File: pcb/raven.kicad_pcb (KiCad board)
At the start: 4 copper layers, 0 parts

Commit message: Finish schematic
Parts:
- added C1: 100u, Capacitor_SMD:C_Elec_8x6.2, F.Cu at (206.4, 74.2)
- added C10: 100n, Capacitor_SMD:C_0402_1005Metric, F.Cu at (135.8, 156.5)
- added C11: 220n, Capacitor_SMD:C_0402_1005Metric, F.Cu at (135.8, 158.5)
- added C12: 4u7, Capacitor_SMD:C_0603_1608Metric, F.Cu at (139.2, 159.3)
- added C13: 100u, Capacitor_SMD:C_Elec_8x6.2, F.Cu at (222.6, 74.2)
- added C14: 100n, Capacitor_SMD:C_0402_1005Metric, F.Cu at (215.4, 66.6)
- added C15: 2u2, Capacitor_SMD:C_0402_1005Metric, F.Cu at (226.4, 65.0)
- added C16: 100n, Capacitor_SMD:C_0402_1005Metric, F.Cu at (216.4, 66.6)
- added C17: 22n, Capacitor_SMD:C_0402_1005Metric, F.Cu at (215.4, 68.6)
- added C18: 100u, Capacitor_SMD:C_Elec_8x6.2, F.Cu at (238.8, 74.2)
- added C19: 100n, Capacitor_SMD:C_0402_1005Metric, F.Cu at (231.6, 66.6)
- added C2: 100n, Capacitor_SMD:C_0402_1005Metric, F.Cu at (199.2, 66.6)
- added C20: 2u2, Capacitor_SMD:C_0402_1005Metric, F.Cu at (242.6, 65.0)
- added C21: 100n, Capacitor_SMD:C_0402_1005Metric, F.Cu at (232.6, 66.6)
- added C22: 22n, Capacitor_SMD:C_0402_1005Metric, F.Cu at (231.6, 68.6)
- added C23: 100u, Capacitor_SMD:C_Elec_8x6.2, F.Cu at (255.0, 74.2)
- added C24: 100n, Capacitor_SMD:C_0402_1005Metric, F.Cu at (247.8, 66.6)
- added C25: 2u2, Capacitor_SMD:C_0402_1005Metric, F.Cu at (258.8, 65.0)
- added C26: 100n, Capacitor_SMD:C_0402_1005Metric, F.Cu at (248.8, 66.6)
- added C27: 22n, Capacitor_SMD:C_0402_1005Metric, F.Cu at (247.8, 68.6)
- added C28: 100n, Capacitor_SMD:C_0402_1005Metric, F.Cu at (89.6, 117.8)
- added C29: 100n, Capacitor_SMD:C_0402_1005Metric, F.Cu at (93.2, 154.5)
- added C3: 2u2, Capacitor_SMD:C_0402_1005Metric, F.Cu at (210.2, 65.0)
- added C30: 100n, Capacitor_SMD:C_0402_1005Metric, F.Cu at (93.2, 156.5)
- added C31: 100n, Capacitor_SMD:C_0402_1005Metric, F.Cu at (93.2, 158.5)
- added C32: 12p, Capacitor_SMD:C_0402_1005Metric, F.Cu at (93.2, 160.4)
- added C33: 12p, Capacitor_SMD:C_0402_1005Metric, F.Cu at (93.2, 162.4)
- added C34: 100n, Capacitor_SMD:C_0402_1005Metric, F.Cu at (93.2, 164.4)
- added C35: 100n, Capacitor_SMD:C_0402_1005Metric, F.Cu at (96.1, 154.5)
- added C36: 100n, Capacitor_SMD:C_0402_1005Metric, F.Cu at (96.1, 156.5)
- added C37: 1u, Capacitor_SMD:C_0402_1005Metric, F.Cu at (96.1, 158.5)
- added C38: 1u, Capacitor_SMD:C_0402_1005Metric, F.Cu at (96.1, 160.4)
- added C39: 100n, Capacitor_SMD:C_0402_1005Metric, F.Cu at (96.1, 162.4)
- added C4: 100n, Capacitor_SMD:C_0402_1005Metric, F.Cu at (200.2, 66.6)
- added C40: 100n, Capacitor_SMD:C_0402_1005Metric, F.Cu at (129.7, 154.5)
- added C41: 100n, Capacitor_SMD:C_0402_1005Metric, F.Cu at (129.7, 156.5)
- added C42: 100n, Capacitor_SMD:C_0402_1005Metric, F.Cu at (129.7, 158.5)
- added C43: 100n, Capacitor_SMD:C_0402_1005Metric, F.Cu at (129.7, 160.4)
- added C44: 100n, Capacitor_SMD:C_0402_1005Metric, F.Cu at (129.7, 162.4)
- added C45: 100n, Capacitor_SMD:C_0402_1005Metric, F.Cu at (155.2, 93.7)
- added C46: 100n, Capacitor_SMD:C_0402_1005Metric, F.Cu at (155.2, 95.7)
- added C47: 100n, Capacitor_SMD:C_0402_1005Metric, F.Cu at (155.2, 97.6)
- added C48: 100n, Capacitor_SMD:C_0402_1005Metric, F.Cu at (155.2, 99.6)
- added C49: 100n, Capacitor_SMD:C_0402_1005Metric, F.Cu at (155.2, 101.6)
- added C5: 22n, Capacitor_SMD:C_0402_1005Metric, F.Cu at (199.2, 68.6)
- added C50: 100n, Capacitor_SMD:C_0402_1005Metric, F.Cu at (108.2, 117.5)
- added C51: 100n, Capacitor_SMD:C_0402_1005Metric, F.Cu at (108.2, 119.5)
- added C52: 100n, Capacitor_SMD:C_0402_1005Metric, F.Cu at (108.2, 121.4)
- added C53: 100n, Capacitor_SMD:C_0402_1005Metric, F.Cu at (108.2, 123.4)
- added C54: 100n, Capacitor_SMD:C_0402_1005Metric, F.Cu at (108.2, 125.4)
- added C55: 100n, Capacitor_SMD:C_0402_1005Metric, F.Cu at (131.7, 117.5)
- added C56: 100n, Capacitor_SMD:C_0402_1005Metric, F.Cu at (131.7, 119.5)
- added C57: 100n, Capacitor_SMD:C_0402_1005Metric, F.Cu at (131.7, 121.4)
- added C58: 100n, Capacitor_SMD:C_0402_1005Metric, F.Cu at (131.7, 123.4)
- added C59: 100n, Capacitor_SMD:C_0402_1005Metric, F.Cu at (131.7, 125.4)
- added C6: 2u2, Capacitor_SMD:C_0402_1005Metric, F.Cu at (86.7, 122.7)
- added C60: 100n, Capacitor_SMD:C_0402_1005Metric, F.Cu at (155.2, 111.4)
- added C61: 100n, Capacitor_SMD:C_0402_1005Metric, F.Cu at (155.2, 113.4)
- added C62: 100n, Capacitor_SMD:C_0402_1005Metric, F.Cu at (155.2, 115.3)
- added C63: 100n, Capacitor_SMD:C_0402_1005Metric, F.Cu at (155.2, 117.3)
- added C64: 100n, Capacitor_SMD:C_0402_1005Metric, F.Cu at (155.2, 119.3)
- added C65: 100u, Capacitor_SMD:C_Elec_8x6.2, F.Cu at (190.2, 74.2)
- added C66: 100n, Capacitor_SMD:C_0402_1005Metric, F.Cu at (183.0, 66.6)
- added C67: 2u2, Capacitor_SMD:C_0402_1005Metric, F.Cu at (194.0, 65.0)
- added C68: 100n, Capacitor_SMD:C_0402_1005Metric, F.Cu at (184.0, 66.6)
- added C69: 22n, Capacitor_SMD:C_0402_1005Metric, F.Cu at (183.0, 68.6)
- added C7: 100n, Capacitor_SMD:C_0402_1005Metric, F.Cu at (86.7, 124.7)
- added C8: 100n, Capacitor_SMD:C_0402_1005Metric, F.Cu at (86.7, 126.7)
- added C9: 2u2, Capacitor_SMD:C_0402_1005Metric, F.Cu at (135.8, 154.5)
- added D1: GLED, LED_SMD:LED_0603_1608Metric, F.Cu at (83.0, 78.6)
- added D10: RLED, LED_SMD:LED_0603_1608Metric, F.Cu at (244.8, 66.8)
- added D11: WLED, LED_SMD:LED_0603_1608Metric, F.Cu at (261.0, 70.0)
- added D12: GLED, LED_SMD:LED_0603_1608Metric, F.Cu at (261.0, 68.4)
- added D13: RLED, LED_SMD:LED_0603_1608Metric, F.Cu at (261.0, 66.8)
- added D14: WLED, LED_SMD:LED_0603_1608Metric, F.Cu at (111.8, 166.4)
- added D15: RLED, LED_SMD:LED_0603_1608Metric, F.Cu at (111.8, 169.0)
- added D16: WLED, LED_SMD:LED_0603_1608Metric, F.Cu at (130.3, 164.7)
- added D17: WLED, LED_SMD:LED_0603_1608Metric, F.Cu at (130.3, 167.3)
- added D18: WLED, LED_SMD:LED_0603_1608Metric, F.Cu at (155.8, 103.8)
- added D19: WLED, LED_SMD:LED_0603_1608Metric, F.Cu at (155.8, 106.4)
- added D2: WLED, LED_SMD:LED_0603_1608Metric, F.Cu at (212.4, 70.0)
- added D20: WLED, LED_SMD:LED_0603_1608Metric, F.Cu at (108.8, 127.7)
- added D21: WLED, LED_SMD:LED_0603_1608Metric, F.Cu at (108.8, 130.2)
- added D22: WLED, LED_SMD:LED_0603_1608Metric, F.Cu at (132.3, 127.7)
- added D23: WLED, LED_SMD:LED_0603_1608Metric, F.Cu at (132.3, 130.2)
- added D24: WLED, LED_SMD:LED_0603_1608Metric, F.Cu at (155.8, 121.5)
- added D25: WLED, LED_SMD:LED_0603_1608Metric, F.Cu at (155.8, 124.1)
- added D26: WLED, LED_SMD:LED_0603_1608Metric, F.Cu at (196.2, 70.0)
- added D27: GLED, LED_SMD:LED_0603_1608Metric, F.Cu at (196.2, 68.4)
- added D28: RLED, LED_SMD:LED_0603_1608Metric, F.Cu at (196.2, 66.8)
- added D3: GLED, LED_SMD:LED_0603_1608Metric, F.Cu at (212.4, 68.4)
- added D4: RLED, LED_SMD:LED_0603_1608Metric, F.Cu at (212.4, 66.8)
- added D5: WLED, LED_SMD:LED_0603_1608Metric, F.Cu at (228.6, 70.0)
- added D6: GLED, LED_SMD:LED_0603_1608Metric, F.Cu at (228.6, 68.4)
- added D7: RLED, LED_SMD:LED_0603_1608Metric, F.Cu at (228.6, 66.8)
- added D8: WLED, LED_SMD:LED_0603_1608Metric, F.Cu at (244.8, 70.0)
- added D9: GLED, LED_SMD:LED_0603_1608Metric, F.Cu at (244.8, 68.4)
- added FB1: FerriteBead, Inductor_SMD:L_0805_2012Metric, F.Cu at (94.1, 171.2)
- added H1: MountingHole_Pad, MountingHole:MountingHole_2.5mm_Pad, F.Cu at (40.0, 50.0)
- added H2: MountingHole_Pad, MountingHole:MountingHole_2.5mm_Pad, F.Cu at (98.0, 50.0)
- added H3: MountingHole_Pad, MountingHole:MountingHole_2.5mm_Pad, F.Cu at (116.2, 93.7)
- added H4: MountingHole_Pad, MountingHole:MountingHole_2.5mm_Pad, F.Cu at (116.2, 100.2)
- added J1: Conn_02x20_Odd_Even, Connector_PinHeader_2.54mm:PinHeader_2x20_P2.54mm_Vertical, F.Cu at (44.9, 51.3)
- added J10: Conn_01x02_Pin, Connector_PinHeader_2.54mm:PinHeader_1x02_P2.54mm_Vertical, F.Cu at (76.0, 124.1)
- added J11: Screw_Terminal_01x02, TerminalBlock_Phoenix:TerminalBlock_Phoenix_MKDS-1,5-2_1x02_P5.00mm_Horizontal, F.Cu at (223.4, 58.1)
- added J12: Screw_Terminal_01x02, TerminalBlock_Phoenix:TerminalBlock_Phoenix_MKDS-1,5-2_1x02_P5.00mm_Horizontal, F.Cu at (239.6, 58.1)
- added J13: Screw_Terminal_01x02, TerminalBlock_Phoenix:TerminalBlock_Phoenix_MKDS-1,5-2_1x02_P5.00mm_Horizontal, F.Cu at (255.8, 58.1)
- added J14: Conn_01x04_Pin, Connector_PinHeader_2.54mm:PinHeader_1x04_P2.54mm_Vertical, F.Cu at (123.0, 155.9)
- added J15: Conn_01x04_Pin, Connector_PinHeader_2.54mm:PinHeader_1x04_P2.54mm_Vertical, F.Cu at (148.5, 95.0)
- added J16: Conn_01x04_Pin, Connector_PinHeader_2.54mm:PinHeader_1x04_P2.54mm_Vertical, F.Cu at (101.5, 118.8)
- added J17: Conn_01x04_Pin, Connector_PinHeader_2.54mm:PinHeader_1x04_P2.54mm_Vertical, F.Cu at (125.0, 118.8)
- added J18: Conn_01x04_Pin, Connector_PinHeader_2.54mm:PinHeader_1x04_P2.54mm_Vertical, F.Cu at (148.5, 112.7)
- added J19: Screw_Terminal_01x02, TerminalBlock_Phoenix:TerminalBlock_Phoenix_MKDS-1,5-2_1x02_P5.00mm_Horizontal, F.Cu at (191.0, 58.3)
- added J2: Conn_01x04_MountingPin, Connector_JST:JST_SH_SM04B-SRSS-TB_1x04-1MP_P1.00mm_Horizontal, F.Cu at (85.3, 73.5)
- added J20: Conn_01x02_Pin, Connector_PinHeader_2.54mm:PinHeader_1x02_P2.54mm_Vertical, F.Cu at (148.4, 167.6)
- added J21: Conn_01x03_Pin, Connector_PinHeader_2.54mm:PinHeader_1x03_P2.54mm_Vertical, F.Cu at (162.1, 95.0)
- added J22: Conn_01x03_Pin, Connector_PinHeader_2.54mm:PinHeader_1x03_P2.54mm_Vertical, F.Cu at (136.6, 166.4)
- added J23: Conn_01x03_Pin, Connector_PinHeader_2.54mm:PinHeader_1x03_P2.54mm_Vertical, F.Cu at (76.0, 103.2)
- added J24: Conn_01x03_Pin, Connector_PinHeader_2.54mm:PinHeader_1x03_P2.54mm_Vertical, F.Cu at (162.1, 112.7)
- added J25: Conn_01x03_Pin, Connector_PinHeader_2.54mm:PinHeader_1x03_P2.54mm_Vertical, F.Cu at (155.1, 155.9)
- added J26: Conn_01x03_Pin, Connector_PinHeader_2.54mm:PinHeader_1x03_P2.54mm_Vertical, F.Cu at (148.4, 155.9)
- added J3: Screw_Terminal_01x02, TerminalBlock_Phoenix:TerminalBlock_Phoenix_MKDS-1,5-2_1x02_P5.00mm_Horizontal, F.Cu at (214.8, 100.0)
- added J4: Screw_Terminal_01x02, TerminalBlock_Phoenix:TerminalBlock_Phoenix_MKDS-1,5-2_1x02_P5.00mm_Horizontal, F.Cu at (187.8, 99.2)
- added J5: Screw_Terminal_01x02, TerminalBlock_Phoenix:TerminalBlock_Phoenix_MKDS-1,5-2_1x02_P5.00mm_Horizontal, F.Cu at (207.2, 58.1)
- added J6: Conn_01x02_Pin, Connector_PinHeader_2.54mm:PinHeader_1x02_P2.54mm_Vertical, F.Cu at (82.7, 103.2)
- added J7: Conn_01x02_Pin, Connector_PinHeader_2.54mm:PinHeader_1x02_P2.54mm_Vertical, F.Cu at (155.8, 130.4)
- added J8: Conn_01x02_Pin, Connector_PinHeader_2.54mm:PinHeader_1x02_P2.54mm_Vertical, F.Cu at (76.0, 114.9)
- added J9: Conn_01x02_Pin, Connector_PinHeader_2.54mm:PinHeader_1x02_P2.54mm_Vertical, F.Cu at (144.3, 130.4)
- added Q1: AO3400A, Package_TO_SOT_SMD:SOT-23, F.Cu at (87.5, 103.3)
- added Q2: AO3400A, Package_TO_SOT_SMD:SOT-23, F.Cu at (160.6, 130.5)
- added Q3: AO3400A, Package_TO_SOT_SMD:SOT-23, F.Cu at (80.8, 115.0)
- added Q4: AO3400A, Package_TO_SOT_SMD:SOT-23, F.Cu at (149.0, 130.5)
- added Q5: AO3400A, Package_TO_SOT_SMD:SOT-23, F.Cu at (80.8, 124.2)
- added Q6: AO3400A, Package_TO_SOT_SMD:SOT-23, F.Cu at (153.2, 167.6)
- added R1: 1k, Resistor_SMD:R_0402_1005Metric, F.Cu at (86.4, 78.3)
- added R10: 1k, Resistor_SMD:R_0402_1005Metric, F.Cu at (227.4, 65.0)
- added R11: 1k, Resistor_SMD:R_0402_1005Metric, F.Cu at (226.0, 68.2)
- added R12: 1k, Resistor_SMD:R_0402_1005Metric, F.Cu at (225.4, 65.0)
- added R13: 1k, Resistor_SMD:R_0402_1005Metric, F.Cu at (229.0, 65.4)
- added R14: 1k, Resistor_SMD:R_0402_1005Metric, F.Cu at (242.2, 69.2)
- added R15: 1k, Resistor_SMD:R_0402_1005Metric, F.Cu at (243.6, 65.0)
- added R16: 1k, Resistor_SMD:R_0402_1005Metric, F.Cu at (242.2, 68.2)
- added R17: 1k, Resistor_SMD:R_0402_1005Metric, F.Cu at (241.6, 65.0)
- added R18: 1k, Resistor_SMD:R_0402_1005Metric, F.Cu at (245.2, 65.4)
- added R19: 1k, Resistor_SMD:R_0402_1005Metric, F.Cu at (258.4, 69.2)
- added R2: 1k, Resistor_SMD:R_0402_1005Metric, F.Cu at (209.8, 69.2)
- added R20: 1k, Resistor_SMD:R_0402_1005Metric, F.Cu at (259.8, 65.0)
- added R21: 1k, Resistor_SMD:R_0402_1005Metric, F.Cu at (258.4, 68.2)
- added R22: 1k, Resistor_SMD:R_0402_1005Metric, F.Cu at (257.8, 65.0)
- added R23: 1k, Resistor_SMD:R_0402_1005Metric, F.Cu at (261.4, 65.4)
- added R24: 10k, Resistor_SMD:R_0402_1005Metric, F.Cu at (86.7, 117.8)
- added R25: R_Photo, Resistor_SMD:R_1210_3225Metric, F.Cu at (88.1, 114.7)
- added R26: 1k, Resistor_SMD:R_0402_1005Metric, F.Cu at (108.3, 166.2)
- added R27: 1k, Resistor_SMD:R_0402_1005Metric, F.Cu at (108.3, 168.1)
- added R28: 1k, Resistor_SMD:R_0402_1005Metric, F.Cu at (108.3, 170.1)
- added R29: 1k, Resistor_SMD:R_0402_1005Metric, F.Cu at (126.8, 154.5)
- added R3: 1k, Resistor_SMD:R_0402_1005Metric, F.Cu at (211.2, 65.0)
- added R30: 1k, Resistor_SMD:R_0402_1005Metric, F.Cu at (126.8, 156.5)
- added R31: 1k, Resistor_SMD:R_0402_1005Metric, F.Cu at (126.8, 158.5)
- added R32: 1k, Resistor_SMD:R_0402_1005Metric, F.Cu at (126.8, 160.5)
- added R33: 1k, Resistor_SMD:R_0402_1005Metric, F.Cu at (126.8, 162.5)
- added R34: 1k, Resistor_SMD:R_0402_1005Metric, F.Cu at (126.8, 164.5)
- added R35: 1k, Resistor_SMD:R_0402_1005Metric, F.Cu at (152.3, 93.7)
- added R36: 1k, Resistor_SMD:R_0402_1005Metric, F.Cu at (152.3, 95.7)
- added R37: 1k, Resistor_SMD:R_0402_1005Metric, F.Cu at (152.3, 97.7)
- added R38: 1k, Resistor_SMD:R_0402_1005Metric, F.Cu at (152.3, 99.7)
- added R39: 1k, Resistor_SMD:R_0402_1005Metric, F.Cu at (152.3, 101.7)
- added R4: 1k, Resistor_SMD:R_0402_1005Metric, F.Cu at (209.8, 68.2)
- added R40: 1k, Resistor_SMD:R_0402_1005Metric, F.Cu at (152.3, 103.6)
- added R41: 1k, Resistor_SMD:R_0402_1005Metric, F.Cu at (105.3, 117.5)
- added R42: 1k, Resistor_SMD:R_0402_1005Metric, F.Cu at (105.3, 119.5)
- added R43: 1k, Resistor_SMD:R_0402_1005Metric, F.Cu at (105.3, 121.5)
- added R44: 1k, Resistor_SMD:R_0402_1005Metric, F.Cu at (105.3, 123.5)
- added R45: 1k, Resistor_SMD:R_0402_1005Metric, F.Cu at (105.3, 125.5)
- added R46: 1k, Resistor_SMD:R_0402_1005Metric, F.Cu at (105.3, 127.5)
- added R47: 1k, Resistor_SMD:R_0402_1005Metric, F.Cu at (128.8, 117.5)
- added R48: 1k, Resistor_SMD:R_0402_1005Metric, F.Cu at (128.8, 119.5)
- added R49: 1k, Resistor_SMD:R_0402_1005Metric, F.Cu at (128.8, 121.5)
- added R5: 1k, Resistor_SMD:R_0402_1005Metric, F.Cu at (209.2, 65.0)
- added R50: 1k, Resistor_SMD:R_0402_1005Metric, F.Cu at (128.8, 123.5)
- added R51: 1k, Resistor_SMD:R_0402_1005Metric, F.Cu at (128.8, 125.5)
- added R52: 1k, Resistor_SMD:R_0402_1005Metric, F.Cu at (128.8, 127.5)
- added R53: 1k, Resistor_SMD:R_0402_1005Metric, F.Cu at (152.3, 111.4)
- added R54: 1k, Resistor_SMD:R_0402_1005Metric, F.Cu at (152.3, 113.4)
- added R55: 1k, Resistor_SMD:R_0402_1005Metric, F.Cu at (152.3, 115.4)
- added R56: 1k, Resistor_SMD:R_0402_1005Metric, F.Cu at (152.3, 117.4)
- added R57: 1k, Resistor_SMD:R_0402_1005Metric, F.Cu at (152.3, 119.4)
- added R58: 1k, Resistor_SMD:R_0402_1005Metric, F.Cu at (152.3, 121.3)
- added R59: 1k, Resistor_SMD:R_0402_1005Metric, F.Cu at (193.6, 69.2)
- added R6: 1k, Resistor_SMD:R_0402_1005Metric, F.Cu at (212.8, 65.4)
- added R60: 1k, Resistor_SMD:R_0402_1005Metric, F.Cu at (195.0, 65.0)
- added R61: 1k, Resistor_SMD:R_0402_1005Metric, F.Cu at (193.6, 68.2)
- added R62: 1k, Resistor_SMD:R_0402_1005Metric, F.Cu at (193.0, 65.0)
- added R63: 1k, Resistor_SMD:R_0402_1005Metric, F.Cu at (196.6, 65.4)
- added R7: 2k2, Resistor_SMD:R_0402_1005Metric, F.Cu at (142.7, 159.1)
- added R8: 2k2, Resistor_SMD:R_0402_1005Metric, F.Cu at (142.7, 161.1)
- added R9: 1k, Resistor_SMD:R_0402_1005Metric, F.Cu at (226.0, 69.2)
- added U1: DRV8874PWPR, Package_SO:HTSSOP-16-1EP_4.4x5mm_P0.65mm_EP3.4x5mm_Mask2.46x2.31mm, F.Cu at (204.7, 66.9)
- added U10: 74AUP1G373, Package_TO_SOT_SMD:SOT-363_SC-70-6, F.Cu at (118.6, 155.5)
- added U11: 74AUP1G373, Package_TO_SOT_SMD:SOT-363_SC-70-6, F.Cu at (118.6, 159.5)
- added U12: 74LVC1G08, Package_TO_SOT_SMD:SOT-353_SC-70-5, F.Cu at (118.6, 163.4)
- added U13: 74LVC1G08, Package_TO_SOT_SMD:SOT-353_SC-70-5, F.Cu at (118.6, 167.3)
- added U14: 74AUP1G373, Package_TO_SOT_SMD:SOT-363_SC-70-6, F.Cu at (144.1, 94.7)
- added U15: 74AUP1G373, Package_TO_SOT_SMD:SOT-363_SC-70-6, F.Cu at (144.1, 98.6)
- added U16: 74LVC1G08, Package_TO_SOT_SMD:SOT-353_SC-70-5, F.Cu at (144.1, 102.5)
- added U17: 74LVC1G08, Package_TO_SOT_SMD:SOT-353_SC-70-5, F.Cu at (144.1, 106.5)
- added U18: 74AUP1G373, Package_TO_SOT_SMD:SOT-363_SC-70-6, F.Cu at (97.1, 118.5)
- added U19: 74AUP1G373, Package_TO_SOT_SMD:SOT-363_SC-70-6, F.Cu at (97.1, 122.4)
- added U2: ICM-42688-P, Package_LGA:LGA-14_3x2.5mm_P0.5mm_LayoutBorder3x4y, F.Cu at (90.4, 123.9)
- added U20: 74LVC1G08, Package_TO_SOT_SMD:SOT-353_SC-70-5, F.Cu at (97.1, 126.4)
- added U21: 74LVC1G08, Package_TO_SOT_SMD:SOT-353_SC-70-5, F.Cu at (97.1, 130.3)
- added U22: 74AUP1G373, Package_TO_SOT_SMD:SOT-363_SC-70-6, F.Cu at (120.6, 118.5)
- added U23: 74AUP1G373, Package_TO_SOT_SMD:SOT-363_SC-70-6, F.Cu at (120.6, 122.4)
- added U24: 74LVC1G08, Package_TO_SOT_SMD:SOT-353_SC-70-5, F.Cu at (120.6, 126.4)
- added U25: 74LVC1G08, Package_TO_SOT_SMD:SOT-353_SC-70-5, F.Cu at (120.6, 130.3)
- added U26: 74AUP1G373, Package_TO_SOT_SMD:SOT-363_SC-70-6, F.Cu at (144.1, 112.4)
- added U27: 74AUP1G373, Package_TO_SOT_SMD:SOT-363_SC-70-6, F.Cu at (144.1, 116.3)
- added U28: 74LVC1G08, Package_TO_SOT_SMD:SOT-353_SC-70-5, F.Cu at (144.1, 120.2)
- added U29: 74LVC1G08, Package_TO_SOT_SMD:SOT-353_SC-70-5, F.Cu at (144.1, 124.2)
- added U3: QMC5883L, Package_LGA:LGA-16_3x3mm_P0.5mm, F.Cu at (139.8, 155.8)
- added U30: DRV8874PWPR, Package_SO:HTSSOP-16-1EP_4.4x5mm_P0.65mm_EP3.4x5mm_Mask2.46x2.31mm, F.Cu at (188.5, 66.9)
- added U4: DRV8874PWPR, Package_SO:HTSSOP-16-1EP_4.4x5mm_P0.65mm_EP3.4x5mm_Mask2.46x2.31mm, F.Cu at (220.9, 66.9)
- added U5: DRV8874PWPR, Package_SO:HTSSOP-16-1EP_4.4x5mm_P0.65mm_EP3.4x5mm_Mask2.46x2.31mm, F.Cu at (237.1, 66.9)
- added U6: DRV8874PWPR, Package_SO:HTSSOP-16-1EP_4.4x5mm_P0.65mm_EP3.4x5mm_Mask2.46x2.31mm, F.Cu at (253.3, 66.9)
- added U7: STM32G431CBUx, Package_DFN_QFN:QFN-48-1EP_7x7mm_P0.5mm_EP5.6x5.6mm, F.Cu at (102.2, 169.8)
- added U8: 74HC595, Package_SO:SOIC-16_3.9x9.9mm_P1.27mm, F.Cu at (101.8, 159.4)
- added U9: 74HC595, Package_SO:SOIC-16_3.9x9.9mm_P1.27mm, F.Cu at (110.2, 159.4)
- added Y1: 16MHz, Crystal:Crystal_SMD_3225-4Pin_3.2x2.5mm, F.Cu at (94.4, 167.6)

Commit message: Save progress
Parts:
- removed C18, C23, C65: 100u, Capacitor_SMD:C_Elec_8x6.2
- removed C39, C41, C42, C43, C44, C46, C47, C48, C49, C51, C52, C53, C54, C56, C57, C58, C59, C61, C62, C63, C64: 100n, Capacitor_SMD:C_0402_1005Metric
- removed D14, D17, D18, D19, D20, D21, D22, D23, D24, D25: WLED, LED_SMD:LED_0603_1608Metric
- removed D15: RLED, LED_SMD:LED_0603_1608Metric
- removed J10, J20, J6, J7, J8, J9: Conn_01x02_Pin, Connector_PinHeader_2.54mm:PinHeader_1x02_P2.54mm_Vertical
- removed J12, J13, J19, J5: Screw_Terminal_01x02, TerminalBlock_Phoenix:TerminalBlock_Phoenix_MKDS-1,5-2_1x02_P5.00mm_Horizontal
- removed Q1, Q2, Q3, Q4, Q5, Q6: AO3400A, Package_TO_SOT_SMD:SOT-23
- removed R26, R33, R34, R39, R40, R45, R46, R51, R52, R57, R58: 1k, Resistor_SMD:R_0402_1005Metric
- removed U10, U11, U14, U15, U18, U19, U22, U23, U26, U27: 74AUP1G373, Package_TO_SOT_SMD:SOT-363_SC-70-6
- removed U12, U13, U16, U17, U20, U21, U24, U25, U28, U29: 74LVC1G08, Package_TO_SOT_SMD:SOT-353_SC-70-5
- removed U9: 74HC595, Package_SO:SOIC-16_3.9x9.9mm_P1.27mm
- J1: footprint Connector_PinHeader_2.54mm:PinHeader_2x20_P2.54mm_Vertical -> Connector_PinSocket_2.54mm:PinSocket_2x20_P2.54mm_Vertical; moved to B.Cu
- J11: value Screw_Terminal_01x02 -> Screw_Terminal_01x10; footprint TerminalBlock_Phoenix:TerminalBlock_Phoenix_MKDS-1,5-2_1x02_P5.00mm_Horizontal -> TerminalBlock_Phoenix:TerminalBlock_Phoenix_MKDS-1,5-10_1x10_P5.00mm_Horizontal
- R7, R8: value 2k2 -> 10k
- moved R28 134.9 mm to (127.6, 36.6)
- moved C34 130.8 mm to (122.9, 37.0)
- moved D16 129.8 mm to (109.9, 36.5)
- moved C29 126.9 mm to (123.3, 31.2)
- moved C30 126.9 mm to (123.3, 33.2)
- moved C31 126.9 mm to (123.3, 35.1)
- moved J11 123.2 mm to (106.5, 96.9), turned to 0 degrees
- moved J22 111.9 mm to (138.6, 54.5)
- moved U7 111.1 mm to (119.4, 60.0), turned to 45 degrees
- moved FB1 109.7 mm to (124.9, 65.9), turned to -45 degrees
- moved R7 109.2 mm to (104.4, 56.8), turned to -90 degrees
- moved R8 109.2 mm to (104.4, 58.8), turned to 90 degrees
- moved R23 107.3 mm to (155.3, 81.5), turned to 90 degrees
- moved C12 105.9 mm to (110.0, 57.6), turned to 180 degrees
- moved C11 105.7 mm to (111.2, 55.6), turned to 90 degrees
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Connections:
- net /MotorHub/ERCTL renamed /MotorHub/SCTL
- net /MotorHub/Encoder10/A renamed /MotorHub/Encoder5/A
- net /MotorHub/Encoder10/AIN renamed /MotorHub/Encoder5/AIN
- net /MotorHub/Encoder10/B renamed /MotorHub/Encoder5/B
- net /MotorHub/Encoder10/BIN renamed /MotorHub/Encoder5/BIN
- net /MotorHub/Encoder6/A renamed /MotorHub/Encoder1/A
- net /MotorHub/Encoder6/AIN renamed /MotorHub/Encoder1/AIN
- net /MotorHub/Encoder6/B renamed /MotorHub/Encoder1/B
- net /MotorHub/Encoder6/BIN renamed /MotorHub/Encoder1/BIN
- net /MotorHub/Encoder7/A renamed /MotorHub/Encoder2/A
- net /MotorHub/Encoder7/AIN renamed /MotorHub/Encoder2/AIN
- net /MotorHub/Encoder7/B renamed /MotorHub/Encoder2/B
- net /MotorHub/Encoder7/BIN renamed /MotorHub/Encoder2/BIN
- net /MotorHub/Encoder8/A renamed /MotorHub/Encoder3/A
- net /MotorHub/Encoder8/AIN renamed /MotorHub/Encoder3/AIN
- net /MotorHub/Encoder8/B renamed /MotorHub/Encoder3/B
- net /MotorHub/Encoder8/BIN renamed /MotorHub/Encoder3/BIN
- net /MotorHub/Encoder9/A renamed /MotorHub/Encoder4/A
- net /MotorHub/Encoder9/AIN renamed /MotorHub/Encoder4/AIN
- net /MotorHub/Encoder9/B renamed /MotorHub/Encoder4/B
- net /MotorHub/Encoder9/BIN renamed /MotorHub/Encoder4/BIN
- net /MotorHub/PHDAT renamed /MotorHub/RDAT
- net /MotorHub/SCLK renamed /MotorHub/RCLK
- net /MotorHub/SSV renamed /MotorHub/RSV
- net Net-(U3-C1) renamed /Magnometer/C1
- D16 pad 2: /MotorHub/Encoder6/BLED -> /MotorHub/SLED
- J1 pad 11: /INT0 -> unconnected-(J1-Pin_11-Pad11)
- J1 pad 13: /INT1 -> unconnected-(J1-Pin_13-Pad13)
- J1 pad 22: unconnected-(J1-Pin_22-Pad22) -> /INT0
- J1 pad 7: unconnected-(J1-Pin_7-Pad7) -> /INT1
- J11 pad 1: /MotorHub/LargeMotor3/OUT1 -> /MotorHub/OA1
- J11 pad 2: /MotorHub/LargeMotor3/OUT2 -> /MotorHub/OB1
- R28 pad 2: /MotorHub/ERLED -> /MotorHub/SLED
- U1 pad 10: /MotorHub/LargeMotor2/OUT2 -> /MotorHub/OB2
- U1 pad 8: /MotorHub/LargeMotor2/OUT1 -> /MotorHub/OA2
- U30 pad 10: /MotorHub/LargeMotor1/OUT2 -> /MotorHub/OB1
- U30 pad 8: /MotorHub/LargeMotor1/OUT1 -> /MotorHub/OA1
- U4 pad 10: /MotorHub/LargeMotor3/OUT2 -> /MotorHub/OB3
- U4 pad 8: /MotorHub/LargeMotor3/OUT1 -> /MotorHub/OA3
- U5 pad 10: /MotorHub/LargeMotor4/OUT2 -> /MotorHub/OB4
- U5 pad 8: /MotorHub/LargeMotor4/OUT1 -> /MotorHub/OA4
- U6 pad 10: /MotorHub/LargeMotor5/OUT2 -> /MotorHub/OB5
- U6 pad 8: /MotorHub/LargeMotor5/OUT1 -> /MotorHub/OA5
- U7 pad 22: /MotorHub/SLDAT -> /MotorHub/PH5
- U7 pad 44: /MotorHub/STCTL -> /MotorHub/SL5
- U8 pad 1: /MotorHub/PH2 -> /MotorHub/SL1
- U8 pad 2: /MotorHub/PH3 -> /MotorHub/PH2
- U8 pad 3: /MotorHub/PH4 -> /MotorHub/SL2
- U8 pad 4: /MotorHub/PH5 -> /MotorHub/PH3
- U8 pad 5: /MotorHub/PH6 -> /MotorHub/SL3
- U8 pad 6: /MotorHub/PH7 -> /MotorHub/PH4
- U8 pad 7: /MotorHub/PH8 -> /MotorHub/SL4
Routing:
- net +3V3: track 0.00 -> 37.0 mm, vias 0 -> 5
- net GND: track 0.00 -> 28.6 mm, vias 0 -> 8
- net /SCL: track 0.00 -> 13.5 mm
- net /SDA: track 0.00 -> 12.0 mm, vias 0 -> 1
- net /INT0: track 0.00 -> 10.3 mm
- net /CS0: track 0.00 -> 7.40 mm
- net /MotorHub/LargeMotor5/FLT: track 0.00 -> 5.08 mm
- net /Magnometer/C1: track 0.00 -> 3.72 mm, vias 0 -> 2
- net /MOSI: track 0.00 -> 3.35 mm
- net /SCK: track 0.00 -> 3.28 mm
- net /MotorHub/IR5: track 0.00 -> 3.07 mm
- net /MotorHub/LargeMotor5/VREF: track 0.00 -> 2.85 mm
- net /MotorHub/PH5: track 0.00 -> 2.17 mm
- net /Magnometer/SETP: track 0.00 -> 2.13 mm
- net /MotorHub/SL5: track 0.00 -> 2.03 mm
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- added copper zone on In1.Cu, net GND
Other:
- board outline added: 63.2 x 54.2 mm

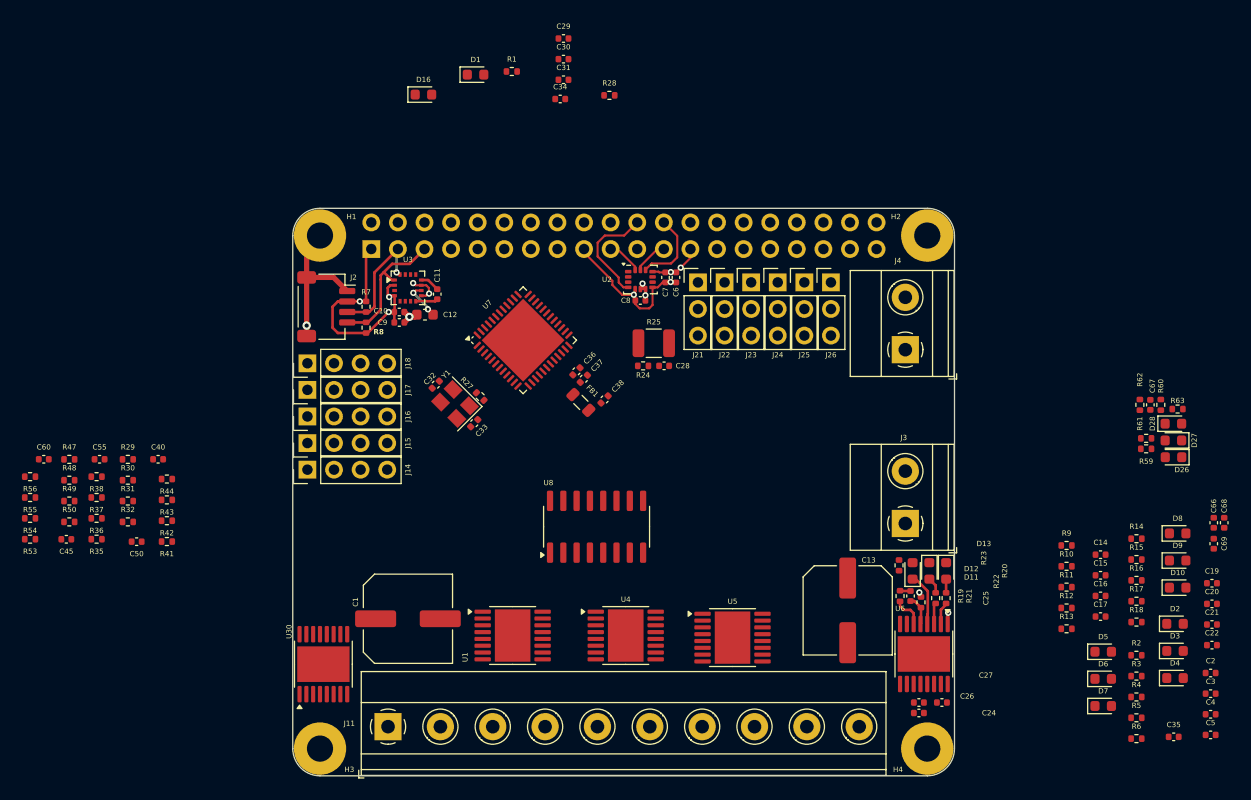
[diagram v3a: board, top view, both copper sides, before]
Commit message: Finish first draft schematic
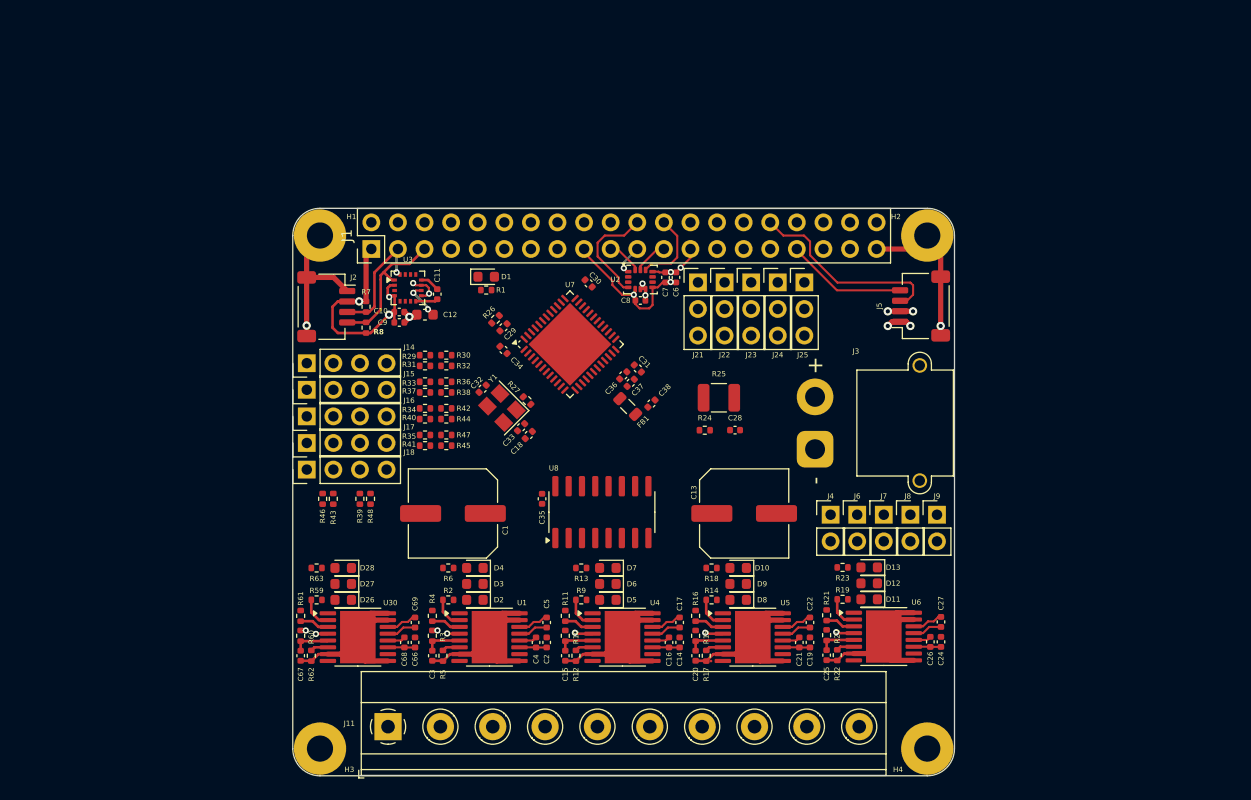
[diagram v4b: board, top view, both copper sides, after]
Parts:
- removed C40, C45, C50, C55, C60: 100n, Capacitor_SMD:C_0402_1005Metric
- removed D16: WLED, LED_SMD:LED_0603_1608Metric
- removed J26: Conn_01x03_Pin, Connector_PinHeader_2.54mm:PinHeader_1x03_P2.54mm_Vertical
- removed R28, R49, R50, R53, R54, R55, R56: 1k, Resistor_SMD:R_0402_1005Metric
- added C18: 100n, Capacitor_SMD:C_0402_1005Metric, F.Cu at (119.9, 69.0)
- added J5: Conn_01x04_MountingPin, Connector_JST:JST_SH_SM04B-SRSS-TB_1x04-1MP_P1.00mm_Horizontal, F.Cu at (157.4, 56.7)
- added J6: Conn_01x02_Pin, Connector_PinHeader_2.54mm:PinHeader_1x02_P2.54mm_Vertical, F.Cu at (151.3, 76.7)
- added J7: Conn_01x02_Pin, Connector_PinHeader_2.54mm:PinHeader_1x02_P2.54mm_Vertical, F.Cu at (153.8, 76.7)
- added J8: Conn_01x02_Pin, Connector_PinHeader_2.54mm:PinHeader_1x02_P2.54mm_Vertical, F.Cu at (156.4, 76.7)
- added J9: Conn_01x02_Pin, Connector_PinHeader_2.54mm:PinHeader_1x02_P2.54mm_Vertical, F.Cu at (158.9, 76.7)
- added R26: 10k, Resistor_SMD:R_0402_1005Metric, F.Cu at (116.8, 58.0)
- added R33: 10k, Resistor_SMD:R_0402_1005Metric, F.Cu at (110.0, 64.0)
- added R34: 10k, Resistor_SMD:R_0402_1005Metric, F.Cu at (110.0, 66.5)
- added R39: 10k, Resistor_SMD:R_0402_1005Metric, F.Cu at (103.8, 75.1)
- added R40: 10k, Resistor_SMD:R_0402_1005Metric, F.Cu at (110.0, 67.5)
- added R45: 10k, Resistor_SMD:R_0402_1005Metric, F.Cu at (112.1, 70.1)
- added R46: 10k, Resistor_SMD:R_0402_1005Metric, F.Cu at (100.3, 75.1)
- J1: footprint Connector_PinSocket_2.54mm:PinSocket_2x20_P2.54mm_Vertical -> Connector_PinHeader_2.54mm:PinHeader_2x20_P2.54mm_Vertical; moved to F.Cu
- J3: value Screw_Terminal_01x02 -> Conn_01x02_Pin; footprint TerminalBlock_Phoenix:TerminalBlock_Phoenix_MKDS-1,5-2_1x02_P5.00mm_Horizontal -> Connector_AMASS:AMASS_XT30PW-M_1x02_P2.50mm_Horizontal
- J4: value Screw_Terminal_01x02 -> Conn_01x02_Pin; footprint TerminalBlock_Phoenix:TerminalBlock_Phoenix_MKDS-1,5-2_1x02_P5.00mm_Horizontal -> Connector_PinHeader_2.54mm:PinHeader_1x02_P2.54mm_Vertical
- R29, R30, R31, R32, R35, R36, R37, R38, R41, R42, R43, R44, R47, R48: value 1k -> 10k
- moved R60 85.1 mm to (98.2, 88.2)
- moved C67 84.6 mm to (98.2, 90.1), turned to -90 degrees
- moved R63 83.6 mm to (99.7, 81.8)
- moved R62 82.7 mm to (99.2, 90.1), turned to 90 degrees
- moved R61 82.5 mm to (98.2, 86.3), turned to -90 degrees
- moved R59 80.5 mm to (99.7, 84.8)
- moved D28 80.5 mm to (102.2, 81.8), turned to 180 degrees
- moved D27 80.5 mm to (102.2, 83.3)
- moved D26 80.5 mm to (102.2, 84.8)
- moved C68 79.1 mm to (108.1, 88.9), turned to 90 degrees
- moved C66 77.1 mm to (109.1, 88.9), turned to 90 degrees
- moved C69 76.7 mm to (109.1, 87.0), turned to -90 degrees
- moved C3 74.4 mm to (110.7, 90.1), turned to -90 degrees
- moved R6 67.7 mm to (112.3, 81.8)
- moved R4 67.7 mm to (110.7, 86.3), turned to -90 degrees
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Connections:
- net /SCL renamed /SCL1
- net /SDA renamed /SDA1
- J1 pad 11: unconnected-(J1-Pin_11-Pad11) -> /BOOT
- J1 pad 12: unconnected-(J1-Pin_12-Pad12) -> /RST
- J1 pad 32: unconnected-(J1-Pin_32-Pad32) -> /SDA2
- J1 pad 33: unconnected-(J1-Pin_33-Pad33) -> /SCL2
- J1 pad 35: unconnected-(J1-Pin_35-Pad35) -> /SW4
- J1 pad 36: unconnected-(J1-Pin_36-Pad36) -> /SW3
- J1 pad 37: unconnected-(J1-Pin_37-Pad37) -> /SW5
- J1 pad 38: unconnected-(J1-Pin_38-Pad38) -> /SW2
- J1 pad 40: unconnected-(J1-Pin_40-Pad40) -> /SW1
- J3 pad 1: VDD -> GND
- J3 pad 2: GND -> VDD
- J4 pad 1: +5V -> GND
- J4 pad 2: GND -> /SW1
- R29 pad 1: /MotorHub/Encoder1/A -> /MotorHub/Encoder1/AIN
- R29 pad 2: /MotorHub/Encoder1/AIN -> /MotorHub/A1
- R30 pad 1: GND -> /MotorHub/A1
- R30 pad 2: /MotorHub/Encoder1/A -> GND
- R31 pad 1: /MotorHub/Encoder1/B -> /MotorHub/Encoder1/BIN
- R31 pad 2: /MotorHub/Encoder1/BIN -> /MotorHub/B1
- R32 pad 1: GND -> /MotorHub/B1
- R32 pad 2: /MotorHub/Encoder1/B -> GND
- R35 pad 1: /MotorHub/Encoder2/A -> /MotorHub/Encoder4/AIN
- R35 pad 2: /MotorHub/Encoder2/AIN -> /MotorHub/A4
- R36 pad 1: GND -> /MotorHub/A2
- R36 pad 2: /MotorHub/Encoder2/A -> GND
- R37 pad 1: /MotorHub/Encoder2/B -> /MotorHub/Encoder2/BIN
- R37 pad 2: /MotorHub/Encoder2/BIN -> /MotorHub/B2
- R38 pad 1: GND -> /MotorHub/B2
- R38 pad 2: /MotorHub/Encoder2/B -> GND
- R41 pad 1: /MotorHub/Encoder3/A -> /MotorHub/Encoder4/BIN
- R41 pad 2: /MotorHub/Encoder3/AIN -> /MotorHub/B4
- R42 pad 1: GND -> /MotorHub/A3
- R42 pad 2: /MotorHub/Encoder3/A -> GND
- R43 pad 1: /MotorHub/Encoder3/B -> /MotorHub/Encoder5/BIN
- R43 pad 2: /MotorHub/Encoder3/BIN -> /MotorHub/B5
- R44 pad 1: GND -> /MotorHub/B3
- R44 pad 2: /MotorHub/Encoder3/B -> GND
- R47 pad 1: /MotorHub/Encoder4/A -> /MotorHub/A4
- R47 pad 2: /MotorHub/Encoder4/AIN -> GND
- R48 pad 1: GND -> /MotorHub/A5
- R48 pad 2: /MotorHub/Encoder4/A -> GND
- U7 pad 2: /MotorHub/INC4 -> /MotorHub/A4
- U7 pad 25: /MotorHub/AMB -> /MotorHub/RSV
- U7 pad 28: /MotorHub/RSV -> /MotorHub/AMB
- U7 pad 29: /MotorHub/DEC2 -> /MotorHub/B2
- U7 pad 3: /MotorHub/INC5 -> /MotorHub/A5
- U7 pad 34: /MotorHub/DEC4 -> /MotorHub/B4
- U7 pad 36: /MotorHub/SCTL -> /MotorHub/B3
- U7 pad 38: /MotorHub/SIG6 -> /MotorHub/CR3
- U7 pad 4: /MotorHub/DEC1 -> /MotorHub/B1
- U7 pad 41: /MotorHub/INC1 -> /MotorHub/A1
- U7 pad 42: /MotorHub/INC2 -> /MotorHub/A2
- U7 pad 43: /MotorHub/INC3 -> /MotorHub/A3
- U7 pad 45: /MotorHub/DEC5 -> /MotorHub/B5
- U7 pad 46: /MotorHub/CR3 -> /BOOT
- U7 pad 7: /MotorHub/DEC3 -> /RST
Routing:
- net GND: track 28.6 -> 141.0 mm, vias 8 -> 11
- net /SDA2: track 0.00 -> 19.3 mm
- net VDD: track 0.00 -> 13.0 mm
- net /SCL2: track 0.00 -> 11.6 mm
- net /MotorHub/LargeMotor4/VREF: track 0.00 -> 3.54 mm
- net /MotorHub/LargeMotor3/VREF: track 0.00 -> 3.54 mm
- net /MotorHub/LargeMotor2/VREF: track 0.00 -> 3.54 mm
- net /MotorHub/LargeMotor1/VREF: track 0.00 -> 3.54 mm
- net /MotorHub/LargeMotor5/FLT: track 5.08 -> 1.72 mm, vias 0 -> 1
- net /MotorHub/PH4: track 0.00 -> 3.13 mm
- net /MotorHub/PH3: track 0.00 -> 3.13 mm
- net /MotorHub/PH1: track 0.00 -> 3.08 mm
- net /MotorHub/PH2: track 0.00 -> 3.06 mm
- net /MotorHub/LargeMotor3/CPL: track 0.00 -> 2.97 mm
- net /MotorHub/LargeMotor1/CPL: track 0.00 -> 2.97 mm
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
